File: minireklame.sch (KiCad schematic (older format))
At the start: 38 parts, among them IC1 ATXMEGA64A4U-A, P1 CONN_01X02, P10 CONN_01X04, P11 CONN_01X04, P12 CONN_01X04, P13 CONN_01X04, P14 CONN_01X04, P15 CONN_01X04, P16 CONN_01X04, P17 CONN_01X04, P2 CONN_01X04, P3 CONN_01X02, P3 CONN_01X04, P4 CONN_01X04, P5 CONN_01X04, P6 CONN_01X04, P7 CONN_01X04, P8 CONN_01X04, P9 CONN_01X04, U1 TLV1117-33CDCYR, U2 SP3483-EN-L, U3 TLC5955

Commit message: chaning power terminal and renumbering connectors
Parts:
- removed P1: CONN_01X02, symbol CONN_01X02
- added P17: Screw_Terminal_1x02, symbol Screw_Terminal_1x02
- gave numbers to parts that had none: 2
- renumbered P2 to P1, P11 to P10, P12 to P11, P13 to P12, P14 to P13, P15 to P14, P16 to P15, P17 to P16, P3 to P19, P3 to P2, P4 to P3, P5 to P4, P6 to P5, P7 to P6, P8 to P7, P9 to P8, P10 to P9
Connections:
- net GND: now also P17.2
- net VDD: now also P17.1
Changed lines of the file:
@@
 $EndComp
 $Comp
-L CONN_01X04 P2
+L CONN_01X04 P1
 U 1 1 58CAF1DB
 P 6100 950
-F 0 "P2" H 6100 1200 50  0000 C CNN
+F 0 "P1" H 6100 1200 50  0000 C CNN
 F 1 "CONN_01X04" V 6200 950 50  0000 C CNN
 F 2 "" H 6100 950 50  0000 C CNN
@@
 $EndComp
 $Comp
-L CONN_01X04 P4
+L CONN_01X04 P3
 U 1 1 58CAF37B
 P 6600 950
-F 0 "P4" H 6600 1200 50  0000 C CNN
+F 0 "P3" H 6600 1200 50  0000 C CNN
 F 1 "CONN_01X04" V 6700 950 50  0000 C CNN
 F 2 "" H 6600 950 50  0000 C CNN
@@
 $EndComp
 $Comp
-L CONN_01X04 P6
+L CONN_01X04 P5
 U 1 1 58CAF520
 P 7100 950
-F 0 "P6" H 7100 1200 50  0000 C CNN
+F 0 "P5" H 7100 1200 50  0000 C CNN
 F 1 "CONN_01X04" V 7200 950 50  0000 C CNN
 F 2 "" H 7100 950 50  0000 C CNN
@@
 $EndComp
 $Comp
-L CONN_01X04 P10
+L CONN_01X04 P9
 U 1 1 58CAF586
 P 8100 950
-F 0 "P10" H 8100 1200 50  0000 C CNN
+F 0 "P9" H 8100 1200 50  0000 C CNN
 F 1 "CONN_01X04" V 8200 950 50  0000 C CNN
 F 2 "" H 8100 950 50  0000 C CNN
@@
 $EndComp
 $Comp
-L CONN_01X04 P8
+L CONN_01X04 P7
 U 1 1 58CAF70B
 P 7600 950
-F 0 "P8" H 7600 1200 50  0000 C CNN
+F 0 "P7" H 7600 1200 50  0000 C CNN
 F 1 "CONN_01X04" V 7700 950 50  0000 C CNN
 F 2 "" H 7600 950 50  0000 C CNN
@@
 $EndComp
 $Comp
-L CONN_01X04 P12
+L CONN_01X04 P11
 U 1 1 58CAF755
 P 9400 2400
-F 0 "P12" H 9400 2650 50  0000 C CNN
+F 0 "P11" H 9400 2650 50  0000 C CNN
 F 1 "CONN_01X04" V 9500 2400 50  0000 C CNN
 F 2 "" H 9400 2400 50  0000 C CNN
@@
 $EndComp
 $Comp
-L CONN_01X04 P14
+L CONN_01X04 P13
 U 1 1 58CAF7BD
 P 9400 3400
-F 0 "P14" H 9400 3650 50  0000 C CNN
+F 0 "P13" H 9400 3650 50  0000 C CNN
 F 1 "CONN_01X04" V 9500 3400 50  0000 C CNN
 F 2 "" H 9400 3400 50  0000 C CNN
@@
 $EndComp
 $Comp
-L CONN_01X04 P13
+L CONN_01X04 P12
 U 1 1 58CAF8AE
 P 9400 2900
-F 0 "P13" H 9400 3150 50  0000 C CNN
+F 0 "P12" H 9400 3150 50  0000 C CNN
 F 1 "CONN_01X04" V 9500 2900 50  0000 C CNN
 F 2 "" H 9400 2900 50  0000 C CNN
@@
 $EndComp
 $Comp
-L CONN_01X04 P17
+L CONN_01X04 P16
 U 1 1 58CB0843
 P 9400 4900
-F 0 "P17" H 9400 5150 50  0000 C CNN
+F 0 "P16" H 9400 5150 50  0000 C CNN
 F 1 "CONN_01X04" V 9500 4900 50  0000 C CNN
 F 2 "" H 9400 4900 50  0000 C CNN
@@
 $EndComp
 $Comp
-L CONN_01X04 P16
+L CONN_01X04 P15
 U 1 1 58CB08AD
 P 9400 4400
-F 0 "P16" H 9400 4650 50  0000 C CNN
+F 0 "P15" H 9400 4650 50  0000 C CNN
 F 1 "CONN_01X04" V 9500 4400 50  0000 C CNN
 F 2 "" H 9400 4400 50  0000 C CNN
@@
 $EndComp
 $Comp
-L CONN_01X04 P15
+L CONN_01X04 P14
 U 1 1 58CB08FC
 P 9400 3900
-F 0 "P15" H 9400 4150 50  0000 C CNN
+F 0 "P14" H 9400 4150 50  0000 C CNN
 F 1 "CONN_01X04" V 9500 3900 50  0000 C CNN
 F 2 "" H 9400 3900 50  0000 C CNN
@@
 $EndComp
 $Comp
-L CONN_01X04 P11
+L CONN_01X04 P10
 U 1 1 58CB0964
 P 8100 6000
-F 0 "P11" H 8100 6250 50  0000 C CNN
+F 0 "P10" H 8100 6250 50  0000 C CNN
 F 1 "CONN_01X04" V 8200 6000 50  0000 C CNN
 F 2 "" H 8100 6000 50  0000 C CNN
@@
 $EndComp
 $Comp
-L CONN_01X04 P9
+L CONN_01X04 P8
 U 1 1 58CB09BD
 P 7600 6000
-F 0 "P9" H 7600 6250 50  0000 C CNN
+F 0 "P8" H 7600 6250 50  0000 C CNN
 F 1 "CONN_01X04" V 7700 6000 50  0000 C CNN
 F 2 "" H 7600 6000 50  0000 C CNN
@@
 $EndComp
 $Comp
-L CONN_01X04 P7
+L CONN_01X04 P6
 U 1 1 58CB0A2B
 P 7100 6000
-F 0 "P7" H 7100 6250 50  0000 C CNN
+F 0 "P6" H 7100 6250 50  0000 C CNN
 F 1 "CONN_01X04" V 7200 6000 50  0000 C CNN
 F 2 "" H 7100 6000 50  0000 C CNN
@@
 $EndComp
 $Comp
-L CONN_01X04 P5
+L CONN_01X04 P4
 U 1 1 58CB0A90
 P 6600 6000
-F 0 "P5" H 6600 6250 50  0000 C CNN
+F 0 "P4" H 6600 6250 50  0000 C CNN
 F 1 "CONN_01X04" V 6700 6000 50  0000 C CNN
 F 2 "" H 6600 6000 50  0000 C CNN
@@
 $EndComp
 $Comp
-L CONN_01X04 P3
+L CONN_01X04 P2
 U 1 1 58CB0B06
 P 6100 6000
-F 0 "P3" H 6100 6250 50  0000 C CNN
+F 0 "P2" H 6100 6250 50  0000 C CNN
 F 1 "CONN_01X04" V 6200 6000 50  0000 C CNN
 F 2 "" H 6100 6000 50  0000 C CNN
@@
 $EndComp
 $Comp
-L CONN_01X02 P3
+L CONN_01X02 P19
 U 1 1 58CB0C3E
 P 850 3750
-F 0 "P3" H 850 3900 50  0000 C CNN
+F 0 "P19" H 850 3900 50  0000 C CNN
 F 1 "CONN_01X02" V 950 3750 50  0000 C CNN
 F 2 "" H 850 3750 50  0000 C CNN
@@
 $EndComp
 $Comp
-L CONN_01X02 P1
-U 1 1 58DE3846
-P 850 1500
-F 0 "P1" H 850 1650 50  0000 C CNN
-F 1 "CONN_01X02" V 950 1500 50  0000 C CNN
-F 2 "" H 850 1500 50  0000 C CNN
-F 3 "" H 850 1500 50  0000 C CNN
-	1    850  1500
-	-1   0    0    -1
-$EndComp
-$Comp
 L VDD #PWR?
 U 1 1 58DE38AE
-P 1300 1450
-F 0 "#PWR?" H 1300 1300 50  0001 C CNN
-F 1 "VDD" H 1300 1600 50  0000 C CNN
-F 2 "" H 1300 1450 50  0001 C CNN
-F 3 "" H 1300 1450 50  0001 C CNN
-	1    1300 1450
-	1    0    0    -1
-$EndComp
-Wire Wire Line
-	1300 1450 1050 1450
+P 1300 1050
+F 0 "#PWR?" H 1300 900 50  0001 C CNN
+F 1 "VDD" H 1300 1200 50  0000 C CNN
+F 2 "" H 1300 1050 50  0001 C CNN
+F 3 "" H 1300 1050 50  0001 C CNN
+	1    1300 1050
+	1    0    0    -1
+$EndComp
+Wire Wire Line
+	1300 1125 1050 1125
 $Comp
 L GND #PWR?
 U 1 1 58DE3ABF
-P 1300 1550
-F 0 "#PWR?" H 1300 1300 50  0001 C CNN
-F 1 "GND" H 1300 1400 50  0000 C CNN
-F 2 "" H 1300 1550 50  0001 C CNN
-F 3 "" H 1300 1550 50  0001 C CNN
-	1    1300 1550
-	1    0    0    -1
-$EndComp
-Wire Wire Line
-	1050 1550 1300 1550
+P 1300 1400
+F 0 "#PWR?" H 1300 1150 50  0001 C CNN
+F 1 "GND" H 1300 1250 50  0000 C CNN
+F 2 "" H 1300 1400 50  0001 C CNN
+F 3 "" H 1300 1400 50  0001 C CNN
+	1    1300 1400
+	1    0    0    -1
+$EndComp
+Wire Wire Line
+	1050 1325 1300 1325
 Wire Wire Line
 	2850 1450 2850 2450
-Text Notes 850  1750 0    60   ~ 12
+Text Notes 900  1550 0    60   ~ 12
 PWR
 Text Notes 750  2950 0    60   ~ 12
@@
 DMX I/O
 $Comp
-L AVR-PUDI-6 CON?
+L AVR-PUDI-6 P18
 U 1 1 5919E95A
 P 975 2350
-F 0 "CON?" H 895 2590 50  0000 C CNN
+F 0 "P18" H 895 2590 50  0000 C CNN
 F 1 "AVR-PUDI-6" H 765 2105 50  0000 L BNN
 F 2 "AVR-PUDI-6" V 530 2385 50  0001 C CNN
@@
 optional XTAL
 $Comp
-L CONN_01X02 P?
+L CONN_01X02 P20
 U 1 1 591AAFD2
 P 850 4275
-F 0 "P?" H 850 4425 50  0000 C CNN
+F 0 "P20" H 850 4425 50  0000 C CNN
 F 1 "CONN_01X02" V 950 4275 50  0000 C CNN
 F 2 "" H 850 4275 50  0000 C CNN
@@
 Text Notes 600  4600 0    60   ~ 0
 junction close to SP3483
+$Comp
+L Screw_Terminal_1x02 P17
+U 1 1 591AB737
+P 850 1225
+F 0 "P17" H 850 1475 50  0000 C TNN
+F 1 "Screw_Terminal_1x02" V 700 1225 50  0000 C TNN
+F 2 "" H 850 1000 50  0001 C CNN
+F 3 "" H 825 1225 50  0001 C CNN
+	1    850  1225
+	1    0    0    -1
+$EndComp
+Wire Wire Line
+	1300 1050 1300 1125
+Wire Wire Line
+	1300 1325 1300 1400
 $EndSCHEMATC

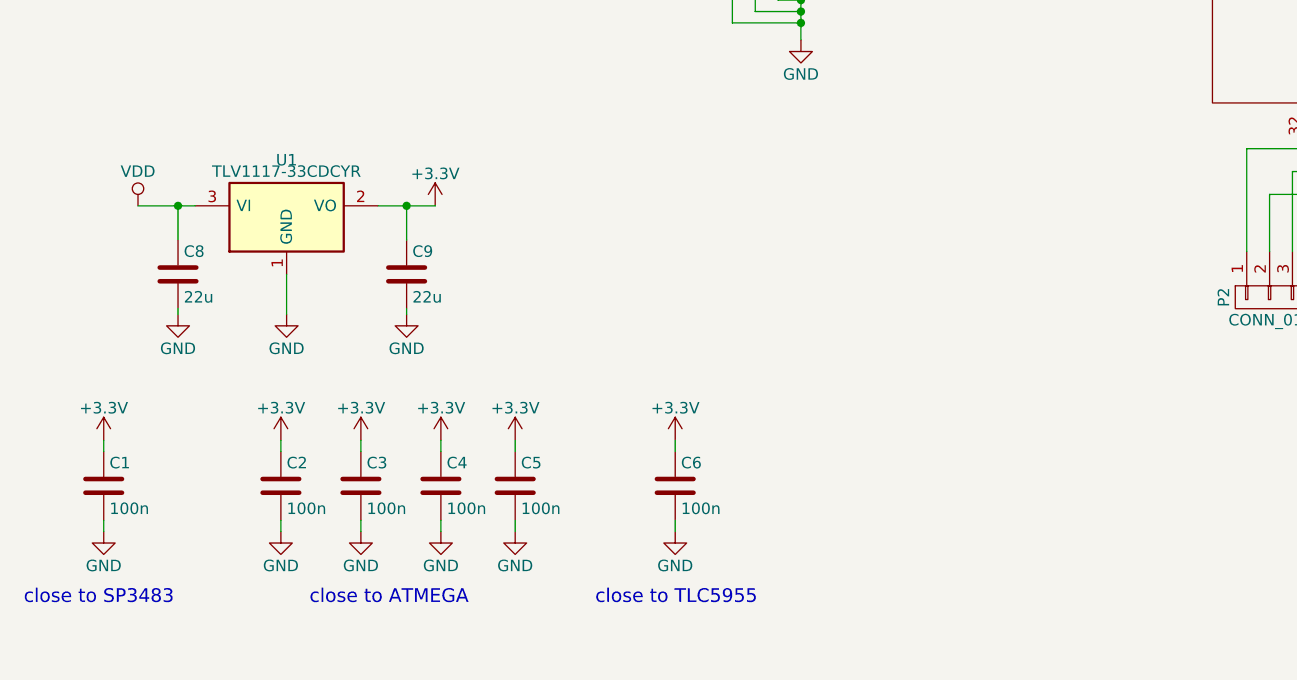
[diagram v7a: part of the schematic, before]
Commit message: support C for VLED
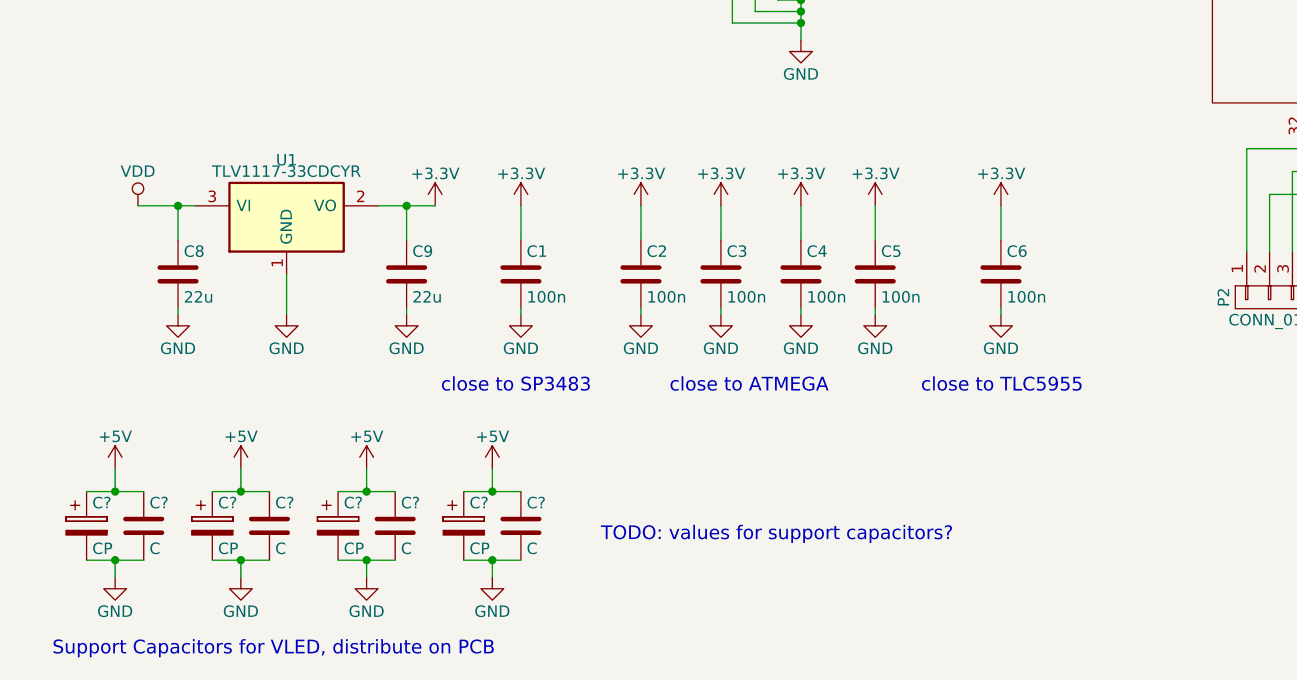
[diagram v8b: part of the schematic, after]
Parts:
- added C? (x4): C, symbol C
- added C? (x4): CP, symbol CP
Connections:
- net +5V: now also C?.1, C?.1, C?.1, C?.1, C?.1, C?.1, C?.1, C?.1
- net GND: now also C?.2, C?.2, C?.2, C?.2, C?.2, C?.2, C?.2, C?.2
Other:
- note added: "Support Capacitors for VLED, distribute on PCB"
- note added: "TODO: values for support capacitors?"
- moved on the sheet: C1, C2, C3, C4, C5, C6
